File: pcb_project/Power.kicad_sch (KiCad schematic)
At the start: 44 parts, among them IC1 TPS54325PWPR, IC2 TPS54294PWPR, J10 M20-9990246, J11 M20-9990246, J12 M20-9990246, J5 USB_B_Micro, J8 M20-9990246, J9 M20-9990246

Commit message: Fix more footprints and add MicroSD reader 3D model
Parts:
- J10, J11, J12, J8, J9: footprint M20-9990246:HARWIN_M20-9990246 -> Project_Footprints:HARWIN_M20-9990246
- L2: footprint Inductor_SMD:L_Bourns-SRN4018 -> Inductor_SMD:L_Bourns_SRP5030T
- L3: footprint (none) -> Inductor_SMD:L_Bourns_SRP5030T
- L4: footprint (none) -> Inductor_SMD:L_Bourns-SRN4018
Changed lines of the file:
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@@
 			)
 		)
-		(property "Footprint" "Inductor_SMD:L_Bourns-SRN4018"
+		(property "Footprint" "Inductor_SMD:L_Bourns_SRP5030T"
 			(at 101.6 118.11 0)
 			(effects
@@
 			)
 		)
-		(property "Footprint" ""
+		(property "Footprint" "Inductor_SMD:L_Bourns-SRN4018"
 			(at 193.04 118.11 0)
 			(effects
@@
 			)
 		)
-		(property "Footprint" "M20-9990246:HARWIN_M20-9990246"
+		(property "Footprint" "Project_Footprints:HARWIN_M20-9990246"
 			(at 251.46 125.73 0)
 			(effects
@@
 			)
 		)
-		(property "Footprint" "M20-9990246:HARWIN_M20-9990246"
+		(property "Footprint" "Project_Footprints:HARWIN_M20-9990246"
 			(at 251.46 97.79 0)
 			(effects
@@
 			)
 		)
-		(property "Footprint" ""
+		(property "Footprint" "Inductor_SMD:L_Bourns_SRP5030T"
 			(at 177.8 48.26 0)
 			(effects
@@
 			)
 		)
-		(property "Footprint" "M20-9990246:HARWIN_M20-9990246"
+		(property "Footprint" "Project_Footprints:HARWIN_M20-9990246"
 			(at 251.46 111.76 0)
 			(effects
@@
 			)
 		)
-		(property "Footprint" "M20-9990246:HARWIN_M20-9990246"
+		(property "Footprint" "Project_Footprints:HARWIN_M20-9990246"
 			(at 251.46 83.82 0)
 			(effects
@@
 			)
 		)
-		(property "Footprint" "M20-9990246:HARWIN_M20-9990246"
+		(property "Footprint" "Project_Footprints:HARWIN_M20-9990246"
 			(at 251.46 69.85 0)
 			(effects

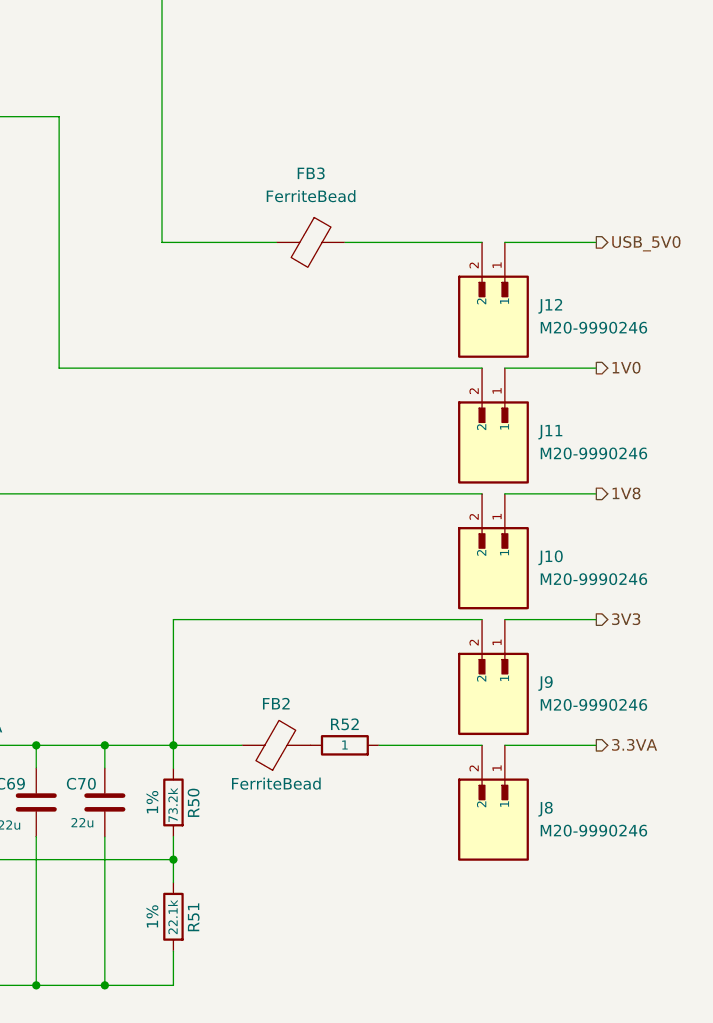
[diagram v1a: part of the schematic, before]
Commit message: Move div layout to use space better and some clean up
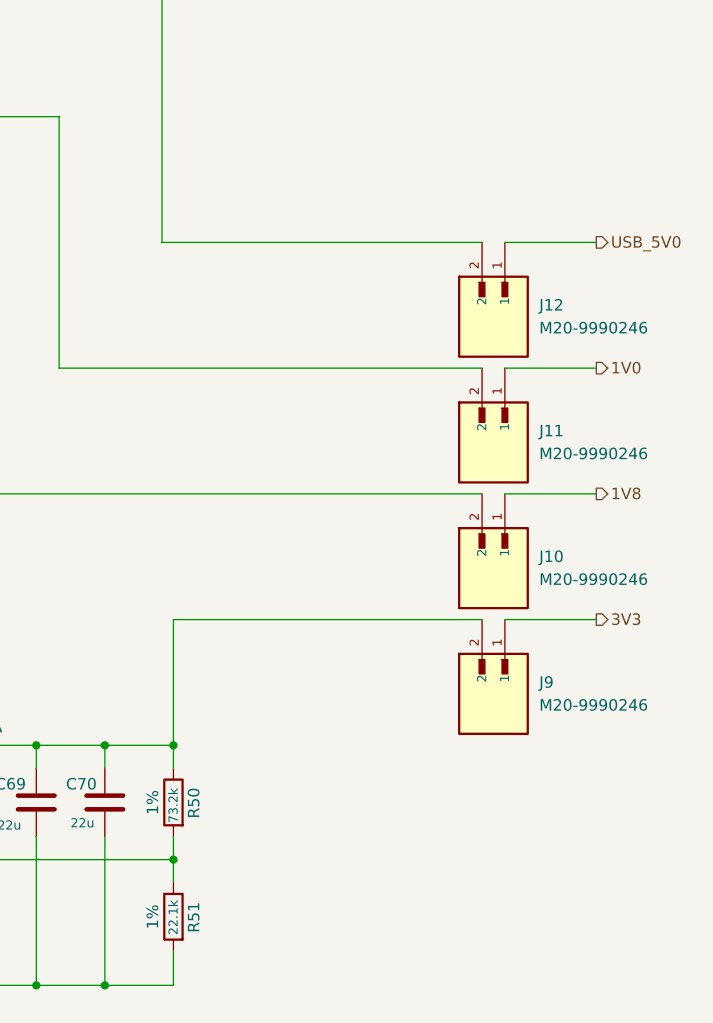
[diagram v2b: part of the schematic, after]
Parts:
- removed FB2, FB3: FerriteBead, Inductor_SMD:L_0805_2012Metric_Pad1.15x1.40mm_HandSolder, symbol Device:FerriteBead
- removed J8: M20-9990246, Project_Footprints:HARWIN_M20-9990246, symbol M20-9990246:M20-9990246
- removed R52: 1, Resistor_SMD:R_0805_2012Metric_Pad1.20x1.40mm_HandSolder, symbol Device:R
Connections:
- net at C54.1, C55.1, C56.1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: now also J12.2

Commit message: Fix power supply layout
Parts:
- IC2: footprint Project_Footprints:SOP65P640X120-15N -> Project_Footprints:SOP65P640X120-17N
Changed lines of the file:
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@@
 			)
 		)
-		(property "Footprint" "Project_Footprints:SOP65P640X120-15N"
+		(property "Footprint" "Project_Footprints:SOP65P640X120-17N"
 			(at 154.94 202.87 0)
 			(effects

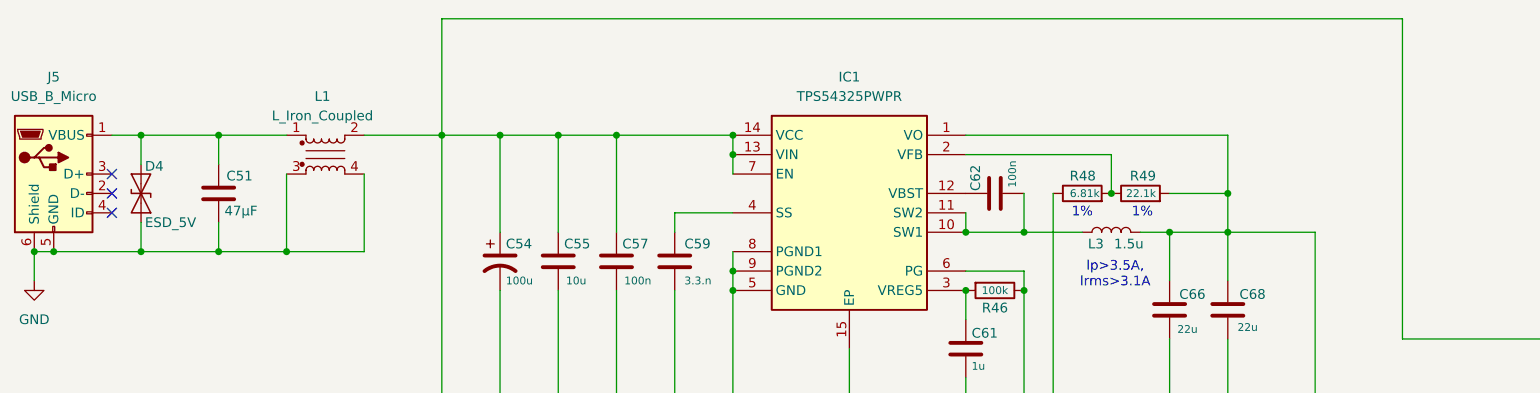
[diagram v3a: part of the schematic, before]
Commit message: Fill ground and pwr layers and connect pins to them
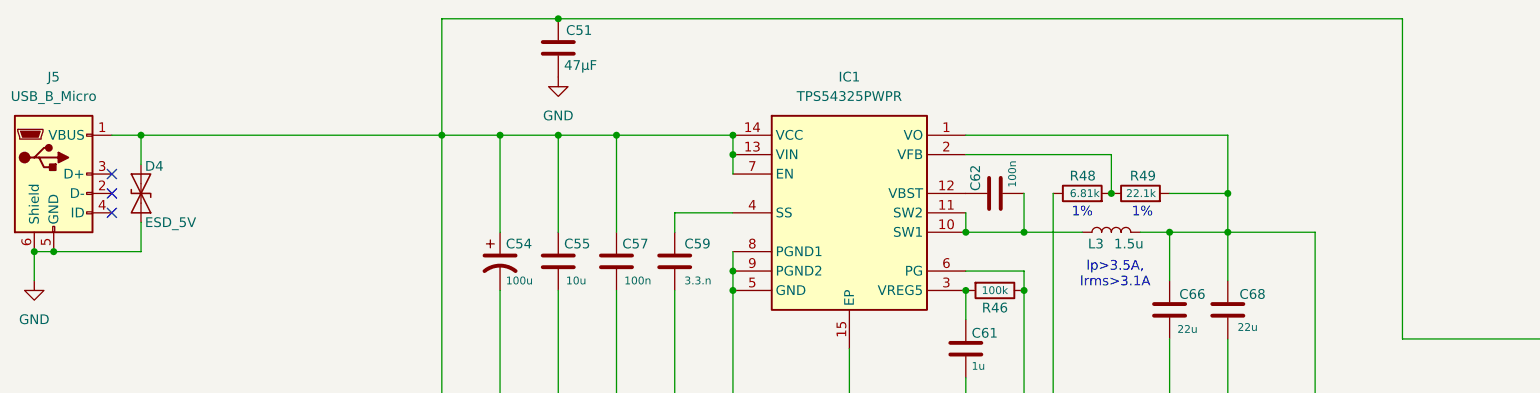
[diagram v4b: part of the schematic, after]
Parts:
- removed L1: L_Iron_Coupled, Inductor_SMD:L_CommonModeChoke_Coilcraft_0805USB, symbol Device:L_Iron_Coupled
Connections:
- net at C51.1, D4.2 (A2), J5.1 (VBUS): now also C54.1, C55.1, C56.1, C57.1, C58.1, C65.1, C67.1, IC1.13 (VIN), IC1.14 (VCC), IC1.7 (EN), IC2.1 (VIN1), IC2.16 (VIN2), J12.2
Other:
- moved on the sheet: C51
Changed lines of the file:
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@@
 	)
 	(junction
+		(at 105.41 20.32)
+		(diameter 0)
+		(color 0 0 0 0)
+	)
+	(junction
 		(at 128.27 69.85)
 		(diameter 0)
@@
 	)
 	(junction
-		(at 60.96 50.8)
-		(diameter 0)
-		(color 0 0 0 0)
-	)
-	(junction
-		(at 69.85 50.8)
-		(diameter 0)
-		(color 0 0 0 0)
-	)
-	(junction
 		(at 115.57 144.78)
 		(diameter 0)
@@
 	)
 	(junction
-		(at 50.8 50.8)
-		(diameter 0)
-		(color 0 0 0 0)
-	)
-	(junction
 		(at 177.8 101.6)
 		(diameter 0)
@@
 	)
 	(junction
-		(at 60.96 35.56)
-		(diameter 0)
-		(color 0 0 0 0)
-	)
-	(junction
 		(at 185.42 144.78)
 		(diameter 0)
@@
 	(wire
 		(pts
-			(xy 50.8 35.56) (xy 60.96 35.56)
-		)
-		(stroke
-			(width 0)
-			(type default)
-		)
-	)
-	(wire
-		(pts
-			(xy 60.96 35.56) (xy 69.85 35.56)
+			(xy 50.8 35.56) (xy 90.17 35.56)
 		)
 		(stroke
@@
 	(wire
 		(pts
-			(xy 215.9 20.32) (xy 90.17 20.32)
-		)
-		(stroke
-			(width 0)
-			(type default)
-		)
-	)
-	(wire
-		(pts
-			(xy 69.85 50.8) (xy 60.96 50.8)
+			(xy 215.9 20.32) (xy 105.41 20.32)
 		)
 		(stroke
@@
 	(wire
 		(pts
-			(xy 69.85 40.64) (xy 69.85 50.8)
-		)
-		(stroke
-			(width 0)
-			(type default)
-		)
-	)
-	(wire
-		(pts
 			(xy 50.8 46.99) (xy 50.8 50.8)
 		)
@@
 	(wire
 		(pts
-			(xy 60.96 35.56) (xy 60.96 39.37)
-		)
-		(stroke
-			(width 0)
-			(type default)
-		)
-	)
-	(wire
-		(pts
 			(xy 113.03 48.26) (xy 113.03 35.56)
 		)
@@
 	(wire
 		(pts
-			(xy 60.96 50.8) (xy 50.8 50.8)
-		)
-		(stroke
-			(width 0)
-			(type default)
-		)
-	)
-	(wire
-		(pts
 			(xy 77.47 128.27) (xy 77.47 130.81)
 		)
@@
 	(wire
 		(pts
-			(xy 80.01 50.8) (xy 69.85 50.8)
-		)
-		(stroke
-			(width 0)
-			(type default)
-		)
-	)
-	(wire
-		(pts
 			(xy 105.41 48.26) (xy 105.41 35.56)
 		)
@@
 	(wire
 		(pts
-			(xy 60.96 46.99) (xy 60.96 50.8)
-		)
-		(stroke
-			(width 0)
-			(type default)
-		)
-	)
-	(wire
-		(pts
 			(xy 107.95 144.78) (xy 115.57 144.78)
 		)
@@
 	(wire
 		(pts
-			(xy 80.01 40.64) (xy 80.01 50.8)
-		)
-		(stroke
-			(width 0)
-			(type default)
-		)
-	)
-	(wire
-		(pts
-			(xy 80.01 35.56) (xy 90.17 35.56)
-		)
-		(stroke
-			(width 0)
-			(type default)
-		)
-	)
-	(wire
-		(pts
 			(xy 77.47 90.17) (xy 77.47 118.11)
 		)
@@
 	(wire
 		(pts
+			(xy 105.41 20.32) (xy 90.17 20.32)
+		)
+		(stroke
+			(width 0)
+			(type default)
+		)
+	)
+	(wire
+		(pts
 			(xy 128.27 53.34) (xy 128.27 55.88)
 		)
@@
 	)
 	(symbol
-		(lib_id "Device:L_Iron_Coupled")
-		(at 74.93 38.1 0)
-		(unit 1)
-		(exclude_from_sim no)
-		(in_bom yes)
-		(on_board yes)
-		(dnp no)
-		(fields_autoplaced yes)
-		(property "Reference" "L1"
-			(at 74.549 30.48 0)
-			(effects
-				(font
-					(size 1.27 1.27)
-				)
-			)
-		)
-		(property "Value" "L_Iron_Coupled"
-			(at 74.549 33.02 0)
-			(effects
-				(font
-					(size 1.27 1.27)
-				)
-			)
-		)
-		(property "Footprint" "Inductor_SMD:L_CommonModeChoke_Coilcraft_0805USB"
-			(at 74.93 38.1 0)
-			(effects
-				(font
-					(size 1.27 1.27)
-				)
-				(hide yes)
-			)
-		)
-		(property "Datasheet" "~"
-			(at 74.93 38.1 0)
-			(effects
-				(font
-					(size 1.27 1.27)
-				)
-				(hide yes)
-			)
-		)
-		(property "Description" "Coupled inductor with iron core"
-			(at 74.93 38.1 0)
-			(effects
-				(font
-					(size 1.27 1.27)
-				)
-				(hide yes)
-			)
-		)
-		(pin "1"
-		)
-		(pin "3"
-		)
-		(pin "2"
-		)
-		(pin "4"
-		)
-		(instances
-			(project "pcb_project"
-				(path "/98f80f66-4595-4d0f-90ca-59b2db6f447b/ce445763-774c-4caf-b911-9c6f9b75d87a"
-					(reference "L1")
-					(unit 1)
-				)
-			)
-		)
-	)
-	(symbol
 		(lib_id "Device:C")
 		(at 193.04 58.42 0)
@@
 	)
 	(symbol
+		(lib_id "power:GND")
+		(at 105.41 27.94 0)
+		(unit 1)
+		(exclude_from_sim no)
+		(in_bom yes)
+		(on_board yes)
+		(dnp no)
+		(fields_autoplaced yes)
+		(property "Reference" "#PWR0136"
+			(at 105.41 34.29 0)
+			(effects
+				(font
+					(size 1.27 1.27)
+				)
+				(hide yes)
+			)
+		)
+		(property "Value" "GND"
+			(at 105.41 33.02 0)
+			(effects
+				(font
+					(size 1.27 1.27)
+				)
+			)
+		)
+		(property "Footprint" ""
+			(at 105.41 27.94 0)
+			(effects
+				(font
+					(size 1.27 1.27)
+				)
+				(hide yes)
+			)
+		)
+		(property "Datasheet" ""
+			(at 105.41 27.94 0)
+			(effects
+				(font
+					(size 1.27 1.27)
+				)
+				(hide yes)
+			)
+		)
+		(property "Description" "Power symbol creates a global label with name \"GND\" , ground"
+			(at 105.41 27.94 0)
+			(effects
+				(font
+					(size 1.27 1.27)
+				)
+				(hide yes)
+			)
+		)
+		(pin "1"
+		)
+		(instances
+			(project ""
+				(path "/98f80f66-4595-4d0f-90ca-59b2db6f447b/ce445763-774c-4caf-b911-9c6f9b75d87a"
+					(reference "#PWR0136")
+					(unit 1)
+				)
+			)
+		)
+	)
+	(symbol
 		(lib_id "Device:C")
 		(at 105.41 52.07 0)
@@
 	(symbol
 		(lib_id "Device:C")
-		(at 60.96 43.18 0)
+		(at 105.41 24.13 0)
 		(unit 1)
 		(exclude_from_sim no)
@@
 		(dnp no)
 		(property "Reference" "C51"
-			(at 61.976 40.894 0)
+			(at 106.426 21.844 0)
 			(effects
 				(font
@@
 		)
 		(property "Value" "47μF"
-			(at 61.722 45.466 0)
+			(at 106.172 26.416 0)
 			(effects
 				(font
@@
 		)
 		(property "Footprint" "Capacitor_SMD:C_1210_3225Metric_Pad1.33x2.70mm_HandSolder"
-			(at 61.9252 46.99 0)
+			(at 106.3752 27.94 0)
 			(effects
 				(font
@@
 		)
 		(property "Datasheet" "~"
-			(at 60.96 43.18 0)
+			(at 105.41 24.13 0)
 			(effects
 				(font
@@
 		)
 		(property "Description" "Unpolarized capacitor"
-			(at 60.96 43.18 0)
+			(at 105.41 24.13 0)
 			(effects
 				(font

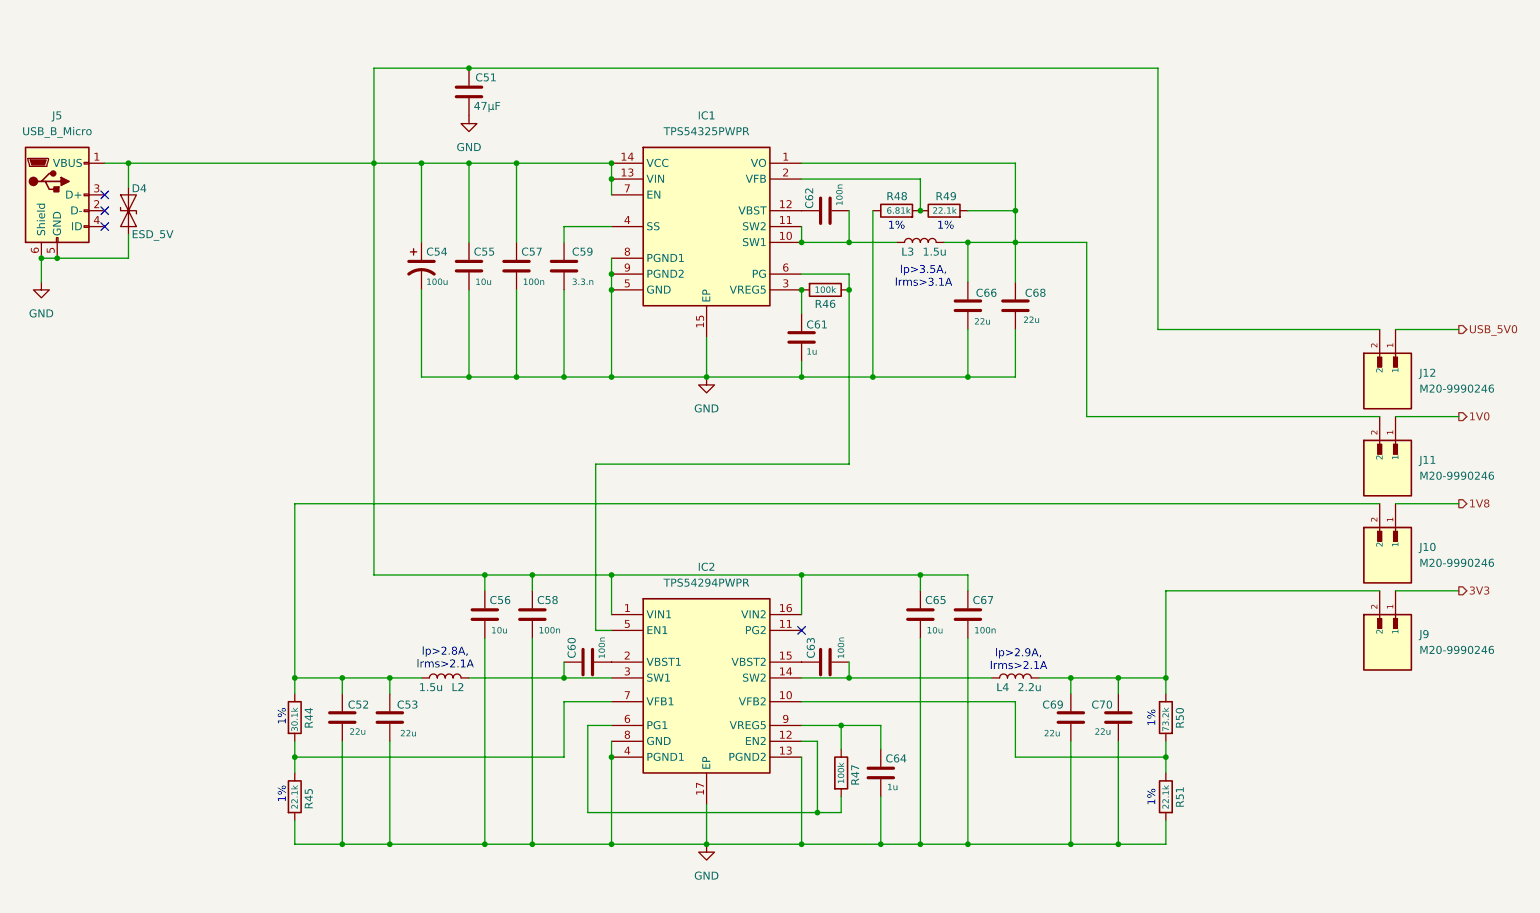
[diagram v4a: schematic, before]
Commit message: Add pwr LEDS, fix FPGA led tranistor values
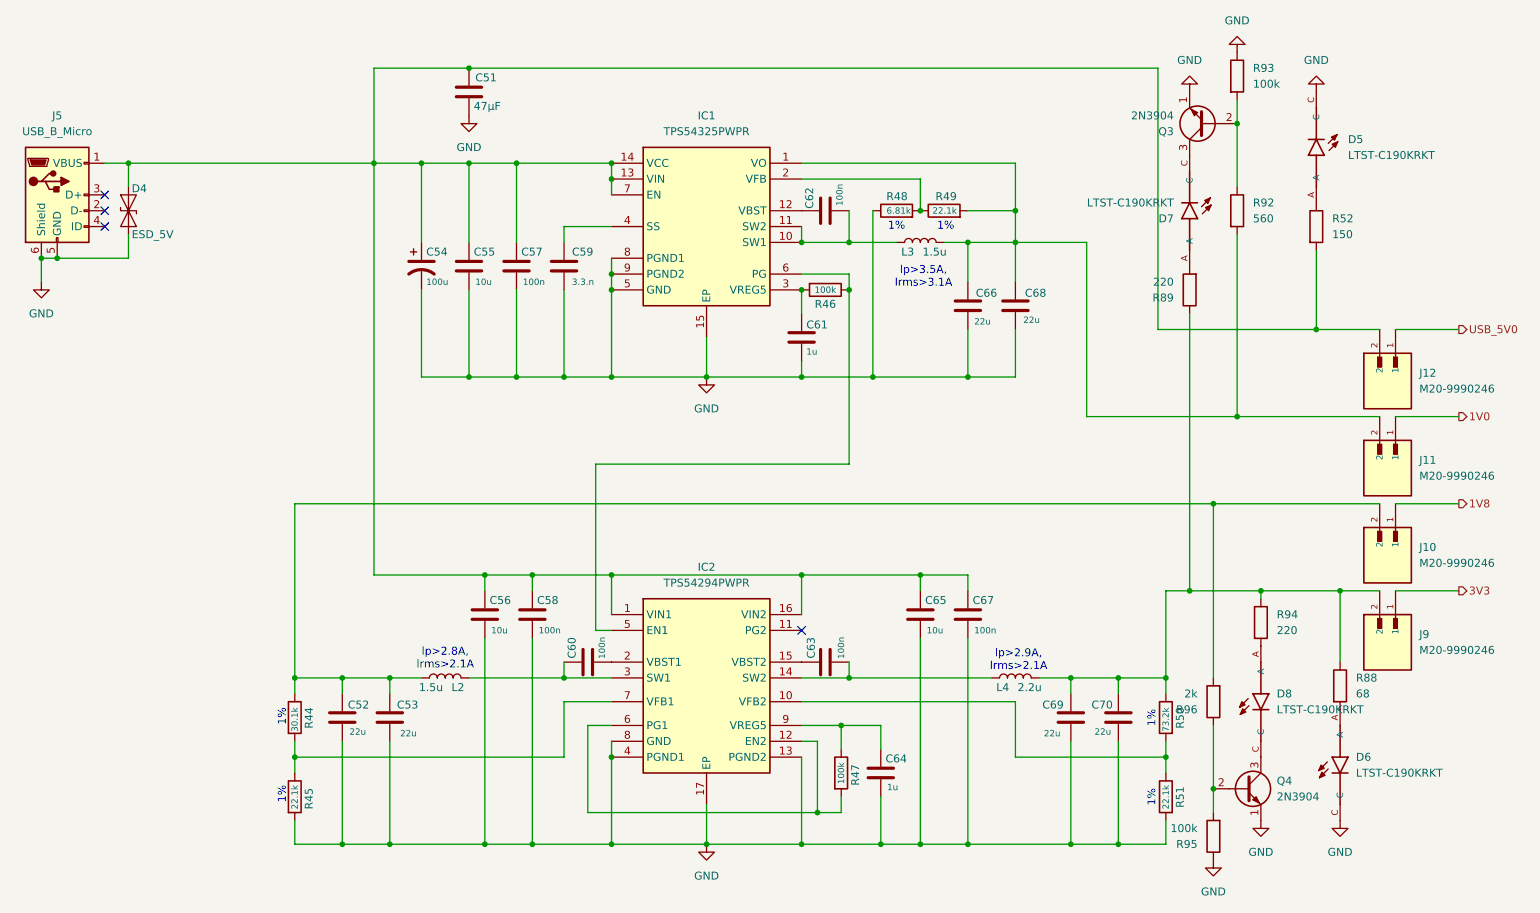
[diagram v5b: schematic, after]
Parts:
- added D5, D6, D7, D8: LTST-C190KRKT, LTST-C190KRKT:LEDC1608X35N, symbol LTST-C190KRKT:LTST-C190KRKT
- added Q3, Q4: 2N3904, Package_TO_SOT_THT:TO-92_Inline, symbol Transistor_BJT:2N3904
- added R52: 150, symbol Device:R
- added R88: 68, symbol Device:R
- added R89, R94: 220, symbol Device:R
- added R92: 560, symbol Device:R
- added R93, R95: 100k, symbol Device:R
- added R96: 2k, symbol Device:R
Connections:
- net GND: now also D5.C, D6.C, Q3.1 (E), Q4.1 (E), R93.1, R95.1
- net at C51.1, C54.1, C55.1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: now also R52.2
- net at C52.1, C53.1, J10.2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: now also R96.2
- net at C69.1, C70.1, J9.2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: now also R88.1, R89.1, R94.1
- net at C66.1, C68.1, IC1.1 (VO)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: now also R92.2
- new net: Q4.2 (B), R95.2, R96.1
- new net: D8.C, Q4.3 (C)
- new net: D6.A, R88.2
- new net: Q3.2 (B), R92.1, R93.2
- new net: D8.A, R94.2
- new net: D7.A, R89.2
- new net: D7.C, Q3.3 (C)
- new net: D5.A, R52.1
